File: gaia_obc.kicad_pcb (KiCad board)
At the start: 6 copper layers, 50 x 50 mm, 150 parts, among them IC1 MAX17048G+T10, J1 USB_C_Receptacle_USB2.0_16P, J2 Conn_02x10_Odd_Even, J3 Conn_02x10_Odd_Even, J4 Conn_01x02_Pin, J5 Micro_SD_Card_Det2, J6 Conn_Coaxial_Small, Q1 FS8205A, Q2 BSS138, SW3 SW_Push, SW4 SW_Push, SW5 SW_Push, SW6 SW_Push, SW7 SW_Push, U1 MCP23017_ML, U10 TPS22917DBV, U11 AP2112K-3.3, U12 DW01A, U13 AP2112K-3.0, U14 LGS4056HDB, U15 CD-PA1616, U16 RFM95W-868S2, U2 USBLC6-2P6, U3 ESP32-S3-PICO-1-N8R2, U4 INA3221, U5 INA3221, U6 TPS22917DBV, U7 TPS22917DBV, U8 TPS22917DBV, U9 TPS22917DBV

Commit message: change screen
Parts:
- removed BZ1: Buzzer, gaia_obc-footprints:buzzer_MLT-5020
- added BZ2: Buzzer, gaia_obc-footprints:buzzer_MLT-5020, F.Cu at (106.0, 108.7)
- added C43: 100nF, Capacitor_SMD:C_0402_1005Metric, F.Cu at (128.0, 110.4)
- added C44: 100nF, Capacitor_SMD:C_0402_1005Metric, F.Cu at (128.0, 112.3)
- added C45: 1uF, Capacitor_SMD:C_0402_1005Metric, F.Cu at (197.4, 101.3)
- added Q3: IRLML6244, Package_TO_SOT_SMD:SOT-23, F.Cu at (111.7, 111.4)
- added R65: 1k, Resistor_SMD:R_0402_1005Metric, F.Cu at (119.0, 116.5)
- added U18: BME280, Package_LGA:Bosch_LGA-8_2.5x2.5mm_P0.65mm_ClockwisePinNumbering, F.Cu at (124.7, 111.7)
- J6: footprint Connector_Coaxial:SMA_Amphenol_132134-10_Vertical -> Connector_Coaxial:SMA_Amphenol_132134_Vertical
- R31, R32, R33, R34, R35, R36: value R_Small -> 0,1
- U17: footprint gaia_obc-footprints:kepernyo -> gaia_obc-footprints:OLED-SMD_ST7735S
- moved J6 130.7 mm to (182.8, 86.4)
- moved J1 62.5 mm to (117.0, 96.6), turned to -45 degrees
- moved U3 51.6 mm to (206.7, 95.6)
- moved J5 39.2 mm to (136.4, 73.1)
- moved U16 33.0 mm to (169.3, 85.4), turned to 0 degrees
- moved U1 26.7 mm to (128.9, 86.8)
- moved U6 22.0 mm to (190.4, 76.6)
- moved SW3 21.7 mm to (170.8, 116.6)
- moved SW4 21.7 mm to (165.3, 111.1)
- moved SW5 21.7 mm to (159.8, 116.6)
- moved SW7 21.7 mm to (165.3, 116.6)
- moved SW6 21.7 mm to (165.3, 122.1)
- moved U17 9.67 mm to (162.9, 100.9)
- moved Q2 9.02 mm to (158.1, 100.5)
- moved U15 6.19 mm to (159.4, 85.3)
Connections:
- J1 pad S1: unconnected-(J1-SHIELD-PadS1)_2 -> GND
- J5 pad 11: unconnected-(J5-SHIELD-Pad11)_3 -> GND

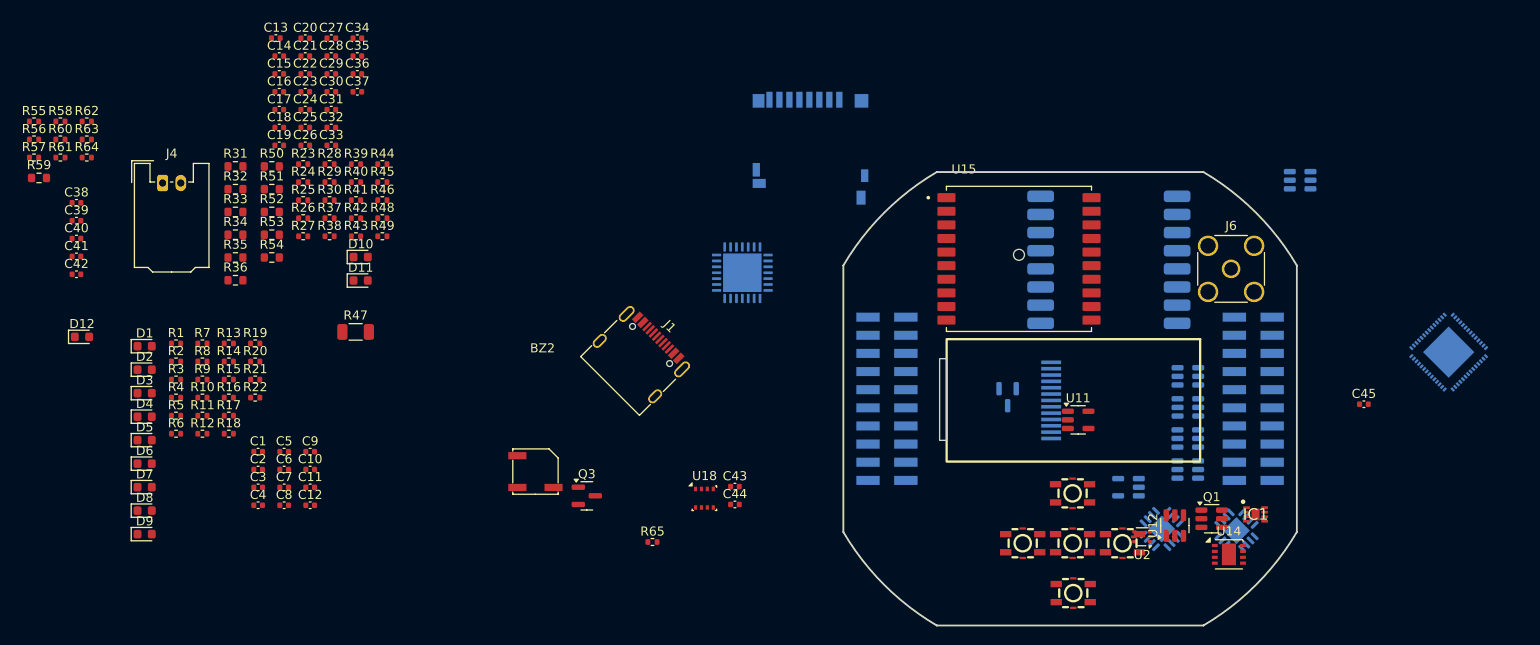
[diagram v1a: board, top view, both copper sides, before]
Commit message: Finalizing schematic+Start placing components
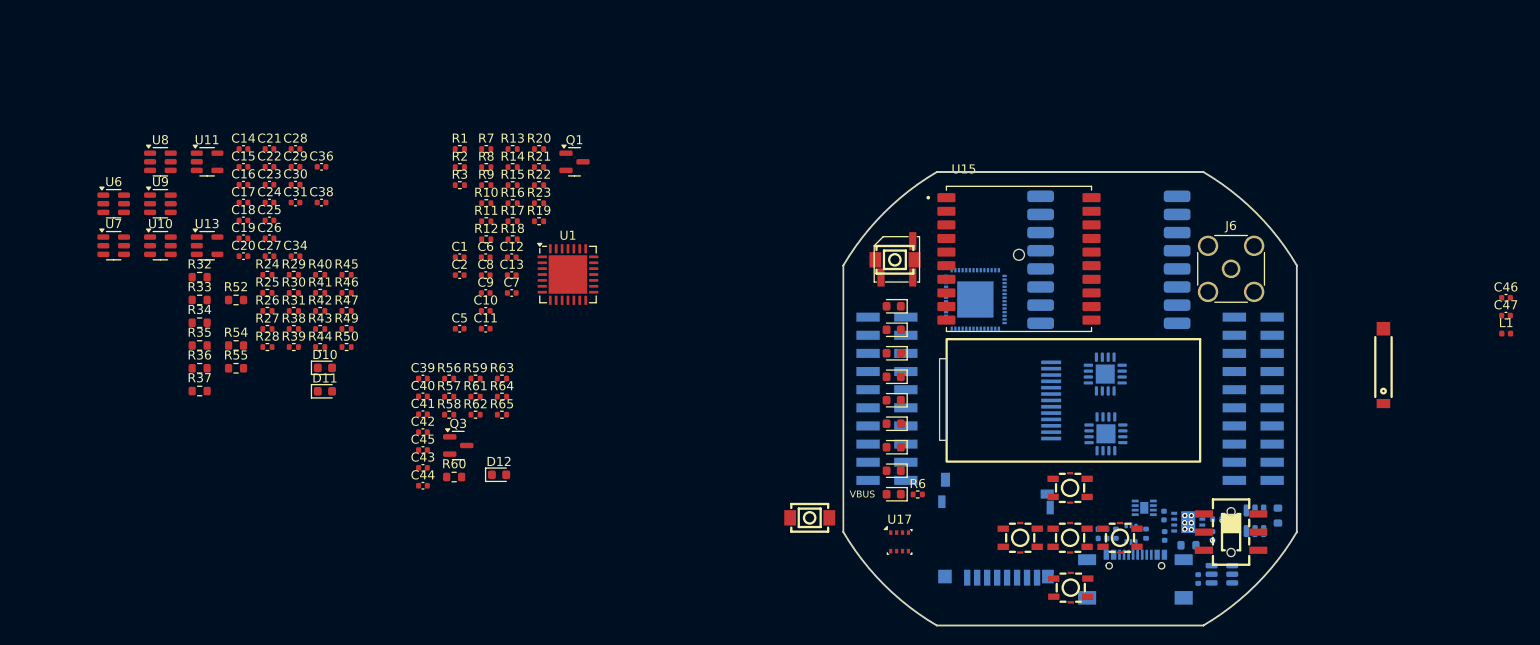
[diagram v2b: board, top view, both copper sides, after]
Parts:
- removed J4: Conn_01x02_Pin, Connector_Molex:Molex_MicroClasp_55935-0230_1x02_P2.00mm_Horizontal
- removed the U18 at (124.7, 111.7)
- added AE1: Antenna, gaia_obc-footprints:ANT-SMD_L8.0-W1.0, F.Cu at (199.6, 97.1)
- added C46: 2,4pF, Capacitor_SMD:C_0402_1005Metric, F.Cu at (213.1, 89.6)
- added C47: 2,0pF, Capacitor_SMD:C_0402_1005Metric, F.Cu at (213.1, 91.5)
- added L1: 2,4nH, Inductor_SMD:L_0402_1005Metric, F.Cu at (213.1, 93.5)
- added SW1: SW_Push, gaia_obc-footprints:KEY-SMD_L4.0-W3.0-LS4.9-1, F.Cu at (145.7, 85.4)
- added SW2: SW_Push, gaia_obc-footprints:KEY-SMD_L4.0-W3.0-LS4.9-1, F.Cu at (136.3, 113.8)
- added SW8: SW_Slide_DPDT, gaia_obc-footprints:MS-22D28-G020, F.Cu at (182.8, 115.4)
- added U17: BME280, Package_LGA:Bosch_LGA-8_2.5x2.5mm_P0.65mm_ClockwisePinNumbering, F.Cu at (146.2, 116.5)
- C12, C25, C41, C45: value 1uF -> 100nF
- C18: value 1nF -> 1uF
- C23: value 1uF -> 1nF
- C24, C31, C38, C42, C7: value 100nF -> 1uF
- C3, C4, IC1, R4, R5, U12, U14, U2: moved to B.Cu
- C32: value 10uF -> 100nF; moved to B.Cu
- C33, C37: value 1uF -> 10uF; moved to B.Cu
- C34: value 10uF -> 1uF
- C35: value 100nF -> 10uF; moved to B.Cu
- C36: value 10uF -> 100nF
- J1: footprint Connector_USB:USB_C_Receptacle_G-Switch_GT-USB-7010ASV -> gaia_obc-footprints:USB-SMD_TYPE-C-16PQT-073; moved to B.Cu
- Q1: value FS8205A -> IRLML6244; footprint Package_TO_SOT_SMD:SOT-23-6 -> Package_TO_SOT_SMD:SOT-23
- Q2: value BSS138 -> FS8205A; footprint Package_TO_SOT_SMD:SOT-23 -> Package_TO_SOT_SMD:SOT-23-6
- Q3: value IRLML6244 -> BSS138
- R19: value 10k -> 1k
- R20: value TBA -> 10k
- R22: value 10k -> TBA
- R31: value 0,1 -> 10k; footprint Resistor_SMD:R_0603_1608Metric -> Resistor_SMD:R_0402_1005Metric
- R37: value 0 -> 0,1; footprint Resistor_SMD:R_0402_1005Metric -> Resistor_SMD:R_0603_1608Metric
- R47: value 100 -> 0; footprint Resistor_SMD:R_1206_3216Metric -> Resistor_SMD:R_0402_1005Metric
- R48: value TBA -> 100; footprint Resistor_SMD:R_0402_1005Metric -> Resistor_SMD:R_0603_1608Metric; moved to B.Cu
- R50: value 1k -> TBA; footprint Resistor_SMD:R_0603_1608Metric -> Resistor_SMD:R_0402_1005Metric
- R51: value 1 -> 1k; moved to B.Cu
- R52: value 1k -> 1
- R53: value 100k -> 1k; footprint Resistor_SMD:R_0603_1608Metric -> Resistor_SMD:R_0402_1005Metric; moved to B.Cu
- R55: value 470 -> 100k; footprint Resistor_SMD:R_0402_1005Metric -> Resistor_SMD:R_0603_1608Metric
- R57: value R_Small -> 470
- R58: value 10k -> R_Small
- R59: value 10 -> 10k; footprint Resistor_SMD:R_0603_1608Metric -> Resistor_SMD:R_0402_1005Metric
- R60: value 10k -> 10; footprint Resistor_SMD:R_0402_1005Metric -> Resistor_SMD:R_0603_1608Metric
- R65: value 1k -> 10k
- U1, U10, U13, U6, U7, U8, U9: moved to F.Cu
- moved U6 130.8 mm to (59.5, 79.2)
- moved U7 119.3 mm to (59.5, 83.8)
- moved R51 116.6 mm to (187.9, 113.6), turned to -90 degrees
- moved U8 116.5 mm to (64.7, 74.6)
- moved U9 116.2 mm to (64.7, 79.2)
- moved U10 115.9 mm to (64.7, 83.8)
- moved R53 108.9 mm to (181.2, 114.0)
- moved C35 108.1 mm to (180.7, 115.8), turned to 90 degrees
- moved R4 108.0 mm to (173.4, 115.6), turned to -90 degrees
- moved C32 107.8 mm to (179.1, 120.6), turned to -90 degrees
- moved U13 105.0 mm to (69.8, 83.8), turned to 0 degrees
- moved R5 104.4 mm to (170.0, 115.6), turned to 90 degrees
- moved C45 103.9 mm to (93.6, 106.3)
- moved C37 101.6 mm to (175.4, 115.8), turned to 90 degrees
- moved C33 100.5 mm to (175.3, 113.6), turned to 90 degrees
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- renumbered BZ2 to BZ1, U17 to U18
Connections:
- BZ1 pad 2: Net-(BZ2--) -> Net-(BZ1--)
- C13 pad 1: GND -> +3.3V
- C13 pad 2: Net-(U4-IN+1) -> GND
- C14 pad 2: Net-(U4-IN+2) -> Net-(U4-IN+1)
- C15 pad 2: Net-(U4-IN+3) -> Net-(U4-IN+2)
- C16 pad 2: Net-(U5-IN+1) -> Net-(U4-IN+3)
- C17 pad 2: Net-(U10-VIN) -> Net-(U5-IN+1)
- C18 pad 1: Net-(U4-IN+1) -> GND
- C18 pad 2: Net-(U6-CT) -> Net-(U10-VIN)
- C19 pad 1: Net-(U4-IN+2) -> Net-(U4-IN+1)
- C19 pad 2: Net-(U7-CT) -> Net-(U6-CT)
- C20 pad 1: Net-(U4-IN+3) -> Net-(U4-IN+2)
- C20 pad 2: Net-(U8-CT) -> Net-(U7-CT)
- C21 pad 1: Net-(U5-IN+1) -> Net-(U4-IN+3)
- C21 pad 2: Net-(U9-CT) -> Net-(U8-CT)
- C22 pad 1: Net-(U10-VIN) -> Net-(U5-IN+1)
- C22 pad 2: Net-(U10-CT) -> Net-(U9-CT)
- C23 pad 1: /Power Supply Unit/OBC_BATT -> Net-(U10-VIN)
- C23 pad 2: GND -> Net-(U10-CT)
- C24 pad 1: +3.3V -> /Power Supply Unit/OBC_BATT
- C25 pad 1: GND -> +3.3V
- C25 pad 2: +3.3V -> GND
- C26 pad 2: /VOUT_A1 -> +3.3V
- C27 pad 2: /VOUT_A2 -> /VOUT_A1
- C28 pad 2: /VOUT_A3 -> /VOUT_A2
- C29 pad 2: /VOUT_B1 -> /VOUT_A3
- C30 pad 2: /VOUT_B2 -> /VOUT_B1
- C31 pad 1: Net-(U12-VCC) -> GND
- C31 pad 2: GND -> /VOUT_B2
- C32 pad 1: GND -> Net-(U12-VCC)
- C32 pad 2: +BATT -> GND
- C33 pad 1: /Power Supply Unit/OBC_BATT -> GND
- C33 pad 2: GND -> +BATT
- C34 pad 1: GND -> /Power Supply Unit/OBC_BATT
- C34 pad 2: Net-(C34-Pad2) -> GND
- C35 pad 1: +3V0 -> GND
- C35 pad 2: GND -> VBUS
- C36 pad 1: GND -> +3V0
- C36 pad 2: +BATT -> GND
- C37 pad 2: +3V0 -> +BATT
- C38 pad 1: +3.3V -> GND
- C38 pad 2: GND -> +3V0
- C39 pad 1: GND -> +3.3V
- C39 pad 2: +3.3V -> GND
- C42 pad 2: +3V0 -> +3.3V
- C45 pad 1: +3.3V -> GND
- C45 pad 2: GND -> +3V0
- J6 pad 1: GND -> Net-(J6-In)
- J6 pad 2: Net-(J6-Ext) -> GND
- Q1 pad 1: GND -> Net-(Q1-G)
- Q1 pad 2: unconnected-(Q1-Pad2)_1 -> GND
- Q1 pad 3: -BATT -> Net-(BZ1--)
- Q2 pad 1: Net-(Q2-G) -> GND
- Q2 pad 2: GND -> unconnected-(Q2-Pad2)_1
- Q2 pad 3: Net-(Q2-D) -> -BATT
- Q3 pad 3: Net-(BZ2--) -> Net-(Q3-D)
- R19 pad 1: I2C_2_SCL -> Net-(U3-GPIO18)
- R19 pad 2: +3.3V -> Net-(Q1-G)
- R20 pad 1: Net-(D8-K) -> I2C_2_SCL
- R20 pad 2: GND -> +3.3V
- R21 pad 1: Net-(D9-K) -> Net-(D8-K)
- R22 pad 1: SPI_0_SCLK -> Net-(D9-K)
- R22 pad 2: +3.3V -> GND
- R23 pad 1: +3.3V -> SPI_0_SCLK
- R23 pad 2: Net-(U4-TC) -> +3.3V
- R24 pad 2: Net-(U5-TC) -> Net-(U4-TC)
- R25 pad 2: Net-(U4-WARNING) -> Net-(U5-TC)
- R26 pad 2: Net-(U5-WARNING) -> Net-(U4-WARNING)
- R27 pad 2: Net-(U4-CRITICAL) -> Net-(U5-WARNING)
- R28 pad 2: Net-(U5-CRITICAL) -> Net-(U4-CRITICAL)
- R29 pad 1: Net-(U4-VPU) -> +3.3V
- R29 pad 2: Net-(U4-PV) -> Net-(U5-CRITICAL)
- R30 pad 1: Net-(U5-VPU) -> Net-(U4-VPU)
- R30 pad 2: Net-(U5-PV) -> Net-(U4-PV)
- R31 pad 1: VCC -> Net-(U5-VPU)
- R31 pad 2: Net-(U4-IN+1) -> Net-(U5-PV)
- R32 pad 2: Net-(U4-IN+2) -> Net-(U4-IN+1)
- R33 pad 2: Net-(U4-IN+3) -> Net-(U4-IN+2)
- R34 pad 2: Net-(U5-IN+1) -> Net-(U4-IN+3)
- R35 pad 2: Net-(U10-VIN) -> Net-(U5-IN+1)
- R36 pad 2: /Power Supply Unit/OBC_BATT -> Net-(U10-VIN)
- R37 pad 1: Net-(U6-QOD) -> VCC
- R37 pad 2: /VOUT_A1 -> /Power Supply Unit/OBC_BATT
- R38 pad 1: Net-(U7-QOD) -> Net-(U6-QOD)
- R38 pad 2: /VOUT_A2 -> /VOUT_A1
- R39 pad 1: Net-(U8-QOD) -> Net-(U7-QOD)
- R39 pad 2: /VOUT_A3 -> /VOUT_A2
- R40 pad 1: Net-(U9-QOD) -> Net-(U8-QOD)
- R40 pad 2: /VOUT_B1 -> /VOUT_A3
- R41 pad 1: Net-(U10-QOD) -> Net-(U9-QOD)
- R41 pad 2: /VOUT_B2 -> /VOUT_B1
- R42 pad 1: GND -> Net-(U10-QOD)
- R42 pad 2: /VOUT_A1 -> /VOUT_B2
- R43 pad 2: /VOUT_A2 -> /VOUT_A1
- R44 pad 2: /VOUT_A3 -> /VOUT_A2
- R45 pad 2: /VOUT_B1 -> /VOUT_A3
- R46 pad 2: /VOUT_B2 -> /VOUT_B1
- R47 pad 1: +BATT -> GND
- R47 pad 2: Net-(U12-VCC) -> /VOUT_B2
- R48 pad 1: Net-(D10-A) -> +BATT
- R48 pad 2: VBUS -> Net-(U12-VCC)
- R49 pad 1: VBUS -> Net-(D10-A)
- R49 pad 2: Net-(D11-A) -> VBUS
- R50 pad 1: -BATT -> VBUS
- R50 pad 2: Net-(U12-CS) -> Net-(D11-A)
- R51 pad 1: Net-(C34-Pad2) -> -BATT
- R51 pad 2: VBUS -> Net-(U12-CS)
- R52 pad 1: Net-(U14-PROG) -> Net-(C35-Pad2)
- R52 pad 2: GND -> VBUS
- R53 pad 1: GND -> Net-(U14-PROG)
- R53 pad 2: Net-(IC1-QSTRT) -> GND
- R54 pad 1: Net-(IC1-~{ALRT}) -> GND
- R54 pad 2: +BATT -> Net-(IC1-QSTRT)
- R55 pad 1: /GPS_TX -> Net-(IC1-~{ALRT})
- R55 pad 2: Net-(U15-TX) -> +BATT
- R56 pad 1: Net-(U15-RX) -> /GPS_TX
- R56 pad 2: /GPS_RX -> Net-(U15-TX)
- R57 pad 1: Net-(D12-K) -> Net-(U15-RX)
- R57 pad 2: GND -> /GPS_RX
- R58 pad 1: +3V0 -> Net-(D12-K)
- R58 pad 2: Net-(Q2-G) -> GND
- R59 pad 1: Net-(Q2-D) -> +3V0
- R59 pad 2: Net-(U17-LEDK) -> Net-(Q3-G)
- R60 pad 1: GND -> Net-(Q3-D)
- R60 pad 2: /PB1 -> Net-(U18-LEDK)
- R61 pad 2: /PB2 -> /PB1
- R62 pad 2: /PB3 -> /PB2
- R63 pad 2: /PB4 -> /PB3
- R64 pad 2: /PB5 -> /PB4
- R65 pad 1: Net-(U3-GPIO18) -> GND
- R65 pad 2: Net-(Q3-G) -> /PB5
- U16 pad 9: Net-(J6-Ext) -> Net-(J6-In)
- U18 pad 11: Net-(U17-LEDK) -> Net-(U18-LEDK)
- U3 pad 1: unconnected-(U3-LNA_IN-Pad1) -> Net-(U3-LNA_IN)
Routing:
- net GND: vias 0 -> 8
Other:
- board text added: "VBUS"

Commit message: finish placing components+small fixes in schema
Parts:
- removed C45: 100nF, Capacitor_SMD:C_0402_1005Metric
- removed R52: 1, Resistor_SMD:R_0603_1608Metric
- AE1, C1, C10, C11, C12, C13, C14, C15, C16, C17, C18, C2, C24, C25, C26, C34, C36, C38, C39, C40, C42, C46, C47, C6, C8, C9, L1, Q3, R1, R13, R14, R15, R16, R17, R18, R2, R20, R23, R24, R25, R26, R27, R28, R29, R3, R30, R31, R54, R55, R56, R57, R59, R60, U1, U10, U11, U13, U6, U7, U8, U9: moved to B.Cu
- R32, R33, R34, R35, R36, R37: footprint Resistor_SMD:R_0603_1608Metric -> Resistor_SMD:R_1206_3216Metric; moved to B.Cu
- moved U6 119.8 mm to (178.2, 95.4)
- moved U7 119.6 mm to (178.2, 98.8)
- moved U8 116.8 mm to (178.2, 102.2)
- moved U9 116.5 mm to (178.2, 105.7)
- moved U10 116.3 mm to (178.2, 109.0)
- moved C23 110.0 mm to (182.2, 108.5), turned to 90 degrees
- moved C22 109.5 mm to (182.2, 104.8), turned to 90 degrees
- moved C21 109.0 mm to (182.2, 100.9), turned to 90 degrees
- moved C20 109.0 mm to (182.2, 97.1), turned to 90 degrees
- moved C19 108.8 mm to (182.2, 93.3), turned to 90 degrees
- moved C31 107.8 mm to (182.7, 110.8), turned to 180 degrees
- moved C30 107.3 mm to (182.7, 107.1), turned to 180 degrees
- moved C29 106.8 mm to (182.7, 103.3), turned to 180 degrees
- moved C27 106.4 mm to (182.6, 95.7), turned to 180 degrees
- moved C28 106.4 mm to (182.7, 99.5), turned to 180 degrees
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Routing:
- net GND: vias 8 -> 38

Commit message: ROUTING 1/3
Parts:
- moved R55 0.80 mm to (176.3, 111.7), turned to 0 degrees
- moved R53 0.72 mm to (180.7, 113.5), turned to 90 degrees
- moved SW8 0.25 mm to (183.0, 115.4)
- moved C33 0.23 mm to (175.3, 113.3)
- moved R28 0.05 mm to (166.2, 94.2), turned to 0 degrees
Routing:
- net VCC: track 0.00 -> 59.3 mm, vias 0 -> 9
- net +BATT: track 0.00 -> 35.5 mm, vias 0 -> 4
- net VBUS: track 0.00 -> 31.6 mm
- net GND: track 0.00 -> 23.2 mm, vias 38 -> 72
- net Net-(U5-IN+1): track 0.00 -> 13.2 mm, vias 0 -> 2
- net Net-(U4-IN+3): track 0.00 -> 12.5 mm
- net Net-(U4-IN+1): track 0.00 -> 12.0 mm
- net Net-(U10-VIN): track 0.00 -> 12.0 mm
- net Net-(U4-IN+2): track 0.00 -> 10.3 mm
- net Net-(U4-PV): track 0.00 -> 8.48 mm, vias 0 -> 2
- net Net-(U5-PV): track 0.00 -> 7.63 mm, vias 0 -> 2
- net Net-(U4-VPU): track 0.00 -> 6.88 mm, vias 0 -> 2
- net Net-(IC1-~{ALRT}): track 0.00 -> 6.31 mm, vias 0 -> 2
- net Net-(U5-VPU): track 0.00 -> 4.94 mm, vias 0 -> 2
- net Net-(IC1-QSTRT): track 0.00 -> 4.54 mm, vias 0 -> 2
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- added copper zone on In2.Cu, net +3.3V
- added copper zone on In1.Cu, net GND
- added copper zone on In4.Cu, net GND

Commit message: ROUTING DONE 08. 24.
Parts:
- added C45: 100nF, Capacitor_SMD:C_0402_1005Metric, B.Cu at (179.0, 92.8)
- added C48: 100nF, Capacitor_SMD:C_0402_1005Metric, B.Cu at (162.5, 107.8)
- C43, C44, U17: moved to B.Cu
- R56, R57: moved to F.Cu
- moved C44 18.8 mm to (157.8, 80.3), turned to 180 degrees
- moved U17 17.7 mm to (158.5, 78.3), turned to 180 degrees
- moved C43 16.5 mm to (159.3, 76.3), turned to 0 degrees
- moved R57 10.9 mm to (148.1, 88.7), turned to 90 degrees
- moved R56 9.56 mm to (149.0, 88.7), turned to -90 degrees
- moved R50 5.51 mm to (144.6, 112.2)
- moved D11 5.36 mm to (141.8, 112.2)
- moved C5 5.05 mm to (174.0, 79.3)
- moved D10 5.03 mm to (141.7, 110.1)
- moved D1 4.95 mm to (141.8, 108.0)
- moved R49 4.90 mm to (144.6, 110.1), turned to 0 degrees
- moved R6 4.89 mm to (144.6, 108.0)
- moved D2 4.68 mm to (141.7, 105.9)
- moved R7 4.59 mm to (144.6, 105.9), turned to 0 degrees
- moved D3 4.41 mm to (141.7, 103.8)
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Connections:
- R49 pad 1: Net-(D10-A) -> Net-(D10-K)
- R50 pad 2: Net-(D11-A) -> Net-(D11-K)
- U1 pad 22: Net-(D5-A) -> Net-(D7-A)
- U1 pad 24: Net-(D7-A) -> Net-(D5-A)
- U1 pad 3: Net-(D3-A) -> Net-(D4-A)
- U1 pad 4: Net-(D4-A) -> Net-(D3-A)
- U14 pad 6: Net-(D11-K) -> Net-(D11-A)
- U14 pad 7: Net-(D10-K) -> Net-(D10-A)
- U3 pad 10: /SCREEN_CS -> /SCREEN_DC
- U3 pad 11: /SCREEN_MOSI -> /SCREEN_CLK
- U3 pad 12: /SCREEN_DC -> /SCREEN_MOSI
- U3 pad 39: /EXP0_USART_TXD -> /EXP2_USART_RXD
- U3 pad 40: /EXP0_USART_RXD -> /EXP2_USART_TXD
- U3 pad 41: /EXP1_SPI_CS -> /EXP0_USART_RXD
- U3 pad 42: /EXP2_USART_TXD -> /EXP0_USART_TXD
- U3 pad 43: /EXP2_USART_RXD -> /EXP1_SPI_CS
- U3 pad 8: /SCREEN_RESET -> /SCREEN_CS
- U3 pad 9: /SCREEN_CLK -> /SCREEN_RESET
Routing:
- net GND: track 23.2 -> 157.3 mm, vias 72 -> 158
- net I2C_1_SDA: track 0.00 -> 133.1 mm, vias 0 -> 12
- net I2C_1_SCL: track 0.00 -> 114.9 mm, vias 0 -> 11
- net +3.3V: track 0.00 -> 74.7 mm, vias 4 -> 33
- net SPI_0_MOSI: track 0.04 -> 63.4 mm, vias 0 -> 7
- net SPI_0_MISO: track 0.00 -> 60.3 mm, vias 0 -> 5
- net SPI_0_SCLK: track 0.00 -> 56.6 mm, vias 0 -> 5
- net /SD_CS: track 0.00 -> 47.6 mm, vias 0 -> 4
- net VBUS: track 31.6 -> 75.8 mm, vias 0 -> 2
- net /EN_A1: track 0.00 -> 41.7 mm, vias 0 -> 2
- net /SCREEN_CS: track 0.00 -> 41.4 mm, vias 0 -> 4
- net Net-(D11-A): track 0.00 -> 40.4 mm, vias 0 -> 2
- net Net-(D10-A): track 0.00 -> 39.1 mm, vias 0 -> 2
- net /EN_A2: track 0.00 -> 37.4 mm, vias 0 -> 2
- net /EN_A3: track 0.00 -> 35.1 mm, vias 0 -> 2
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- added copper zone on B.Cu, net GND
- added copper zone on In6.Cu, net GND
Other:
- copper layers 6 -> 8
- board text removed: "VBUS"

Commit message: fixing minor bugs
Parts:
- C5: moved to B.Cu
- moved C5 17.5 mm to (156.6, 77.6), turned to -90 degrees
- moved SW1 0.70 mm to (175.8, 79.2)
- moved R62 0.50 mm to (165.0, 113.0)
- moved BZ1 0.07 mm to (171.3, 83.1)
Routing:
- net GND: track 157.3 -> 151.8 mm, vias 158 -> 199
- net Net-(U3-CHIP_PU): track 32.6 -> 32.0 mm

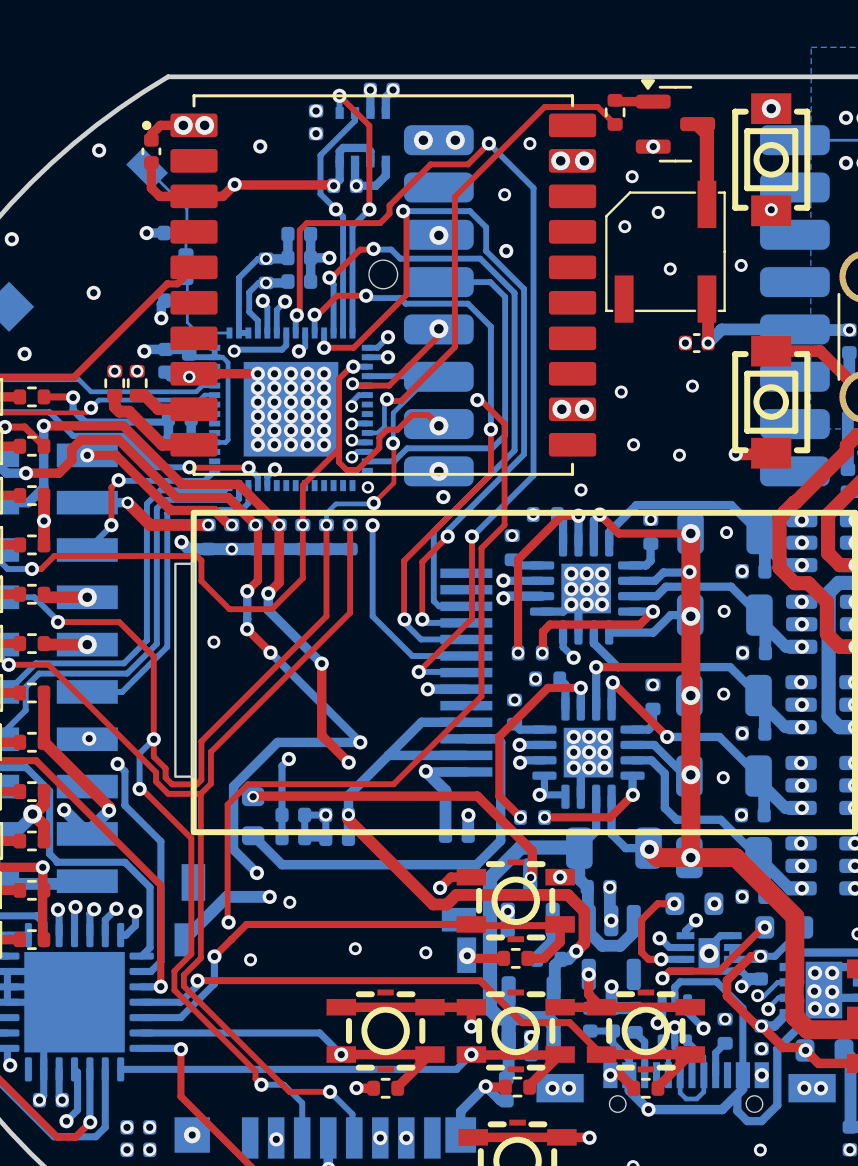
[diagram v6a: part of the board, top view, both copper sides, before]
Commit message: cleaning up footprints + fixing DRC
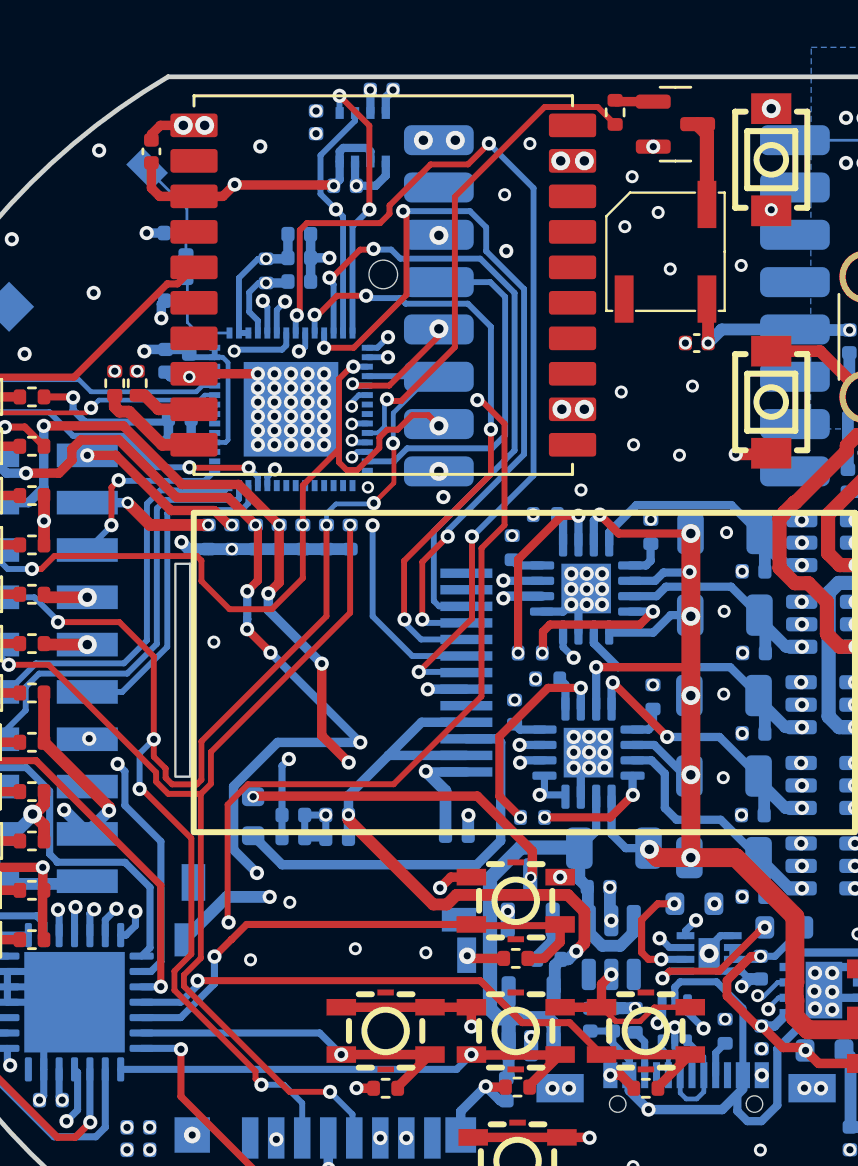
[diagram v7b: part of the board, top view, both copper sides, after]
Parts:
- J2, J3: footprint Connector_PinHeader_2.00mm:PinHeader_2x10_P2.00mm_Vertical_SMD -> gaia_obc-footprints:PinHeader_2x10_P2.00mm_Vertical_SMD
- Q1, Q3: footprint Package_TO_SOT_SMD:SOT-23 -> gaia_obc-footprints:SOT-23
- Q2, U10, U12, U6, U7, U8, U9: footprint Package_TO_SOT_SMD:SOT-23-6 -> gaia_obc-footprints:SOT-23-6
- U1: footprint Package_DFN_QFN:QFN-28-1EP_6x6mm_P0.65mm_EP4.25x4.25mm -> gaia_obc-footprints:QFN-28-1EP_6x6mm_P0.65mm_EP4.25x4.25mm
- U11: footprint Package_TO_SOT_SMD:SOT-23-5 -> gaia_obc-footprints:SOT-23-6
- U13: footprint Package_TO_SOT_SMD:SOT-23-5 -> gaia_obc-footprints:SOT-23-5
- U14: footprint Package_DFN_QFN:DFN-8-1EP_3x3mm_P0.65mm_EP1.55x2.4mm -> gaia_obc-footprints:DFN-8-1EP_3x3mm_P0.65mm_EP1.55x2.4mm
- U16: footprint RF_Module:HOPERF_RFM9XW_SMD -> gaia_obc-footprints:HOPERF_RFM9XW_SMD
- U17: footprint Package_LGA:Bosch_LGA-8_2.5x2.5mm_P0.65mm_ClockwisePinNumbering -> gaia_obc-footprints:Bosch_LGA-8_2.5x2.5mm_P0.65mm_ClockwisePinNumbering
- U2: footprint Package_TO_SOT_SMD:SOT-666 -> gaia_obc-footprints:SOT-666
- U4, U5: footprint Package_DFN_QFN:Texas_RGV0016A_VQFN-16-1EP_4x4mm_P0.65mm_EP2.1x2.1mm -> gaia_obc-footprints:Texas_RGV0016A_VQFN-16-1EP_4x4mm_P0.65mm_EP2.1x2.1mm
